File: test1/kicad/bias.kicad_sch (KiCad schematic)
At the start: 0 parts

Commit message: test1: fill in Power, Bias, Bobcat, Connectors, FMC sheets
Completes the test1 Bobcat carrier hierarchical schematic. All 7 sheets
(root + 6 children) parse cleanly with kicad-cli and render to SVG/PDF.

Contents per child:
  - power.kicad_sch       — TPS7A8401A LDO (3P3V → 0.8V via ANY-OUT
                            strap, OUT side fans to +VDDD/+VDDA1/+VDDA2
                            via 1×2 jumpers) + TPS22916 load switch
                            (VADJ → +VDDIO) with EN pulldowns + decoupling.
  - bobcat.kicad_sch      — Bobcat 40-QFN DUT with VDDD/VDDIO decoupling,
                            VDDA1/VDDA2 series 0Ω + decoupling, hier-label
                            exits on all four edges for SAMPLE_OUT*,
                            SPI, GPIO, CLK_OUT*, BIAS0/1, etc.
  - eeprom.kicad_sch      — 24AA08 I²C EEPROM (address 000, WP→GND,
                            0.1 µF decoupling, 2.2 kΩ I²C pull-ups).
  - bias.kicad_sch        — MCP4728 quad DAC + OPA2388 dual op-amp
                            (units 1 & 2) + PMZ1200UPEYL high-side PMOS
                            × 2 channels + 5.11 kΩ 0.1% sense resistors +
                            DNP 2N7002 isolation NMOS placeholders.
  - connectors.kicad_sch  — 4× SMA for CLK_OUT0–3, 3× SMA for
                            OSC_EN/WEIGHT_EN/SAMPLE_TRIG, 1×4 GPIO
                            header, 3× Keystone-5011 GND test clips.
  - fmc.kicad_sch         — VITA 57.1 LPC connector (4 units × 40 pins),
                            wired for 3P3V/VADJ/SCL/SDA/PRSNT/GA0/GA1/
                            PG_C2M/LDO_EN/LSW_EN; LA-bank pins NC'd for
                            later pinning; all other C/D/G/H pins to GND.

Generator improvements driven by this round:
  - Multi-unit symbol support (parse_pins now returns the per-pin unit
    number; place() takes a unit= parameter and emits matching (unit N)
    in the instance + path).
  - Escape backslash/quote in property values so refs/values with
    embedded " (e.g. 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
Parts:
- added C1, C3, C4: 0.1uF, Capacitor_SMD:C_0402_1005Metric, symbol Device:C
- added C2: 10nF, Capacitor_SMD:C_0402_1005Metric, symbol Device:C
- added Q1, Q2: PMZ1200UPEYL, Package_DFN_QFN:DFN-3-1EP_1.0x1.0mm_P0.65mm_EP0.5x0.5mm, symbol Lib:PMZ1200UPEYL
- added Q3, Q4: 2N7002 (DNP), Package_TO_SOT_SMD:SOT-23, symbol Lib:2N7002
- added R1, R2: 5.11k 0.1%, Resistor_SMD:R_0402_1005Metric, symbol Device:R
- added U1: MCP4728, Package_DFN_QFN:VQFN-10-1EP_3x3mm_P0.5mm_EP1.6x1.6mm, symbol Lib:MCP4728
- added U2: OPA2388, Package_SO:SOIC-8_3.9x4.9mm_P1.27mm, symbol Lib:OPA2388
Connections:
- new net: U1.7 (VOUTB), U2.5 (+IN_B)
- new net: Q2.1 (G), U2.7 (OUT_B)
- new net: Q1.1 (G), U2.1 (OUT_A)
- new net: U1.6 (VOUTA), U2.3 (+IN_A)
- new net +3V3: C1.1, C2.1, C3.1, C4.1, R1.1, R2.1, U1.1 (VDD), U2.8 (V+)
- new net BIAS0: Q1.2 (S), Q1.3 (D), R1.2, U2.2 (-IN_A)
- new net BIAS1: Q2.2 (S), Q2.3 (D), R2.2, U2.6 (-IN_B)
- new net GND: C1.2, C2.2, C3.2, C4.2, U1.10 (VSS), U1.4 (*LDAC), U2.4 (V-)
- new net SCL: U1.2 (SCL)
- new net SDA: U1.3 (SDA)
- no-connect marks 0 -> 9

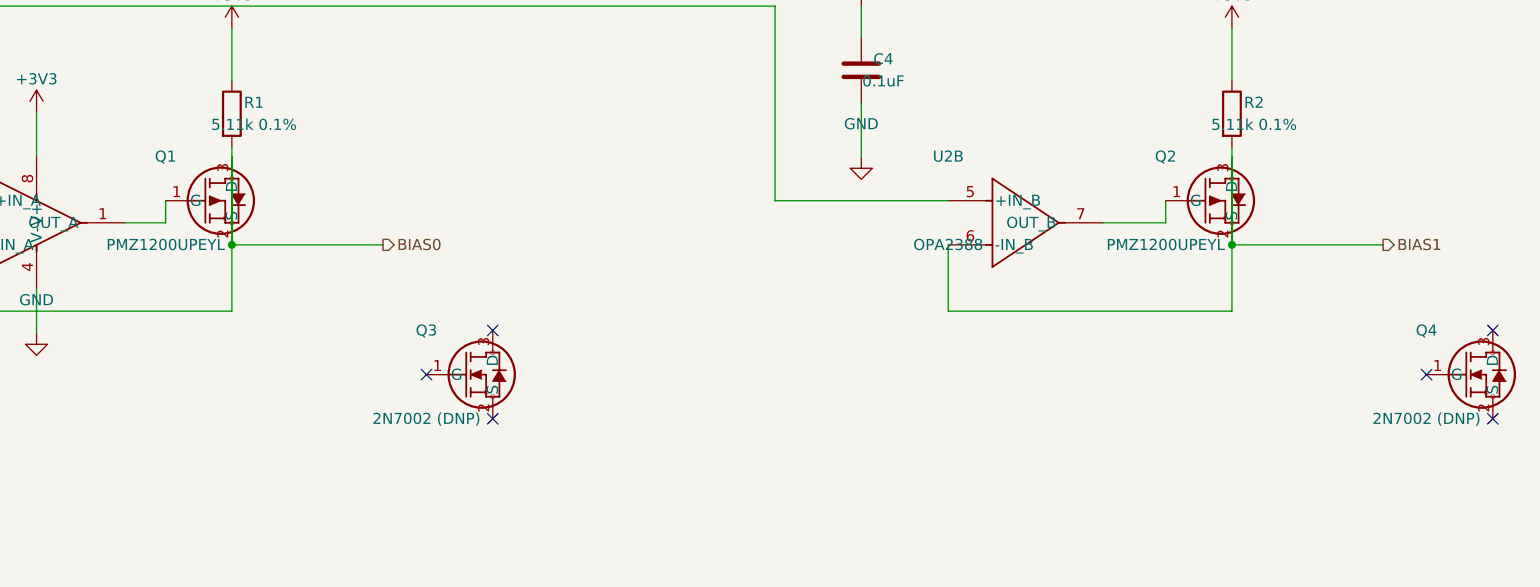
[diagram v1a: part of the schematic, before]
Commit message: Apply layout best-practices from reference schematic
Skill updates (from the LTC3114 reference sample):
  - New rule 5: no net passes through a component body (visual ambiguity).
  - New rule 6: every placed component is in-path or removed — DNP parts
    stay wired in series and just carry (dnp yes) + "DNP" value tag; never
    leave a part with no_connect on all its pins as a "for later"
    placeholder.
  - New rule 7: GND symbols cluster — one (power:GND) per local pin group,
    not one per pin. Connector banks bus their GNDs onto a single rail
    with one terminating triangle.
  - New rule 8: canonical decoupling-cap cluster (bulk+HF share one rail
    above and one GND below; stay off the path of unrelated nets).

test1 design fixes (each addresses a specific point raised on review):

  1. Bias: Q3, Q4 (2N7002 NMOS isolators) now wired in series between
     each PMOS drain and the BIASx output — gates exit as BIAS_ISO0 /
     BIAS_ISO1 hier labels for MCU control. Marked DNP via "2N7002 DNP"
     value. No more orphaned no_connects.

  2. Bobcat: VDDA2 decoupling cap C4 moved onto its own branch BELOW the
     R6 series-0Ω lane, off the pin-26/27 tie wire path.

  3. FMC: ~150 individual per-pin GND symbols collapsed into one
     consolidated GND rail per unit (J1/J2/J3/J4), each terminating in a
     single GND triangle at the rail's bottom.

  4. Power: TPS22916 (U2) decoupling caps C6 and C7 moved ALONGSIDE the
     chip body (left and right) at the same y as VIN/VOUT — wires no
     longer pass under the chip footprint. Cap pin 1 (top) → chip pin
     via horizontal stub; cap pin 2 (bot) → GND rail below.

Co-Authored-By: Claude Opus 4.7 (1M context) <noreply@anthropic.com>
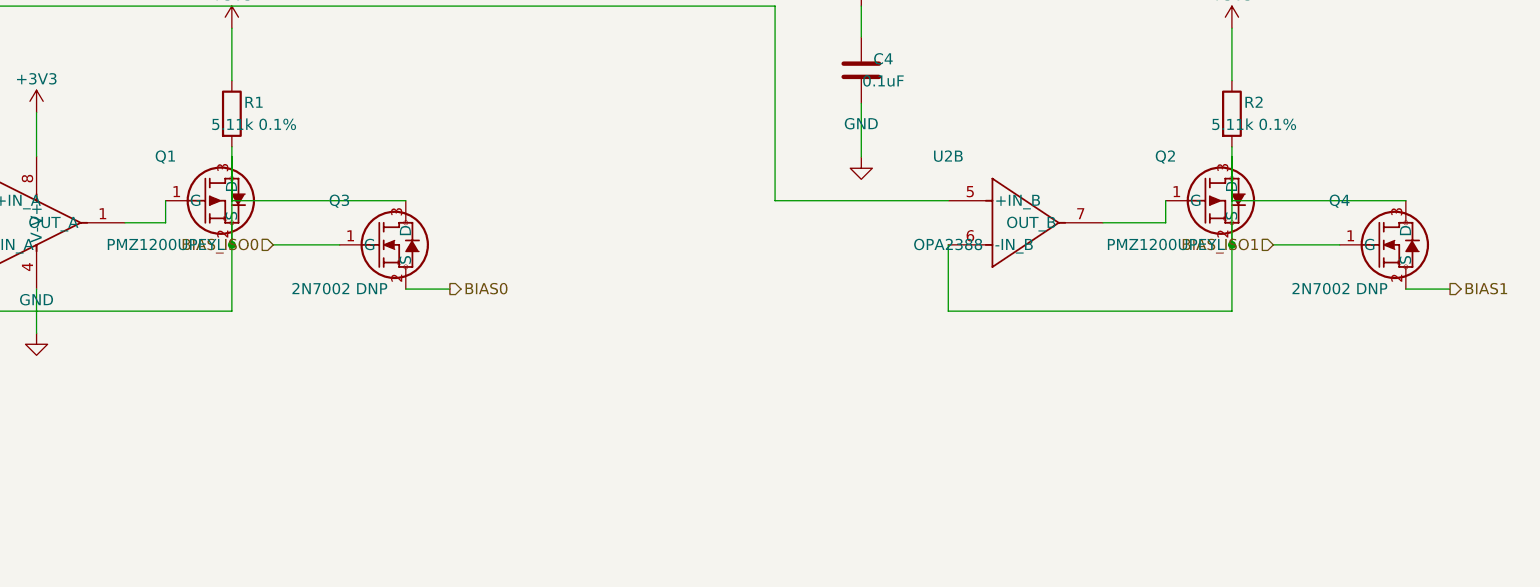
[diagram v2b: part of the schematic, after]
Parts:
- Q3, Q4: value 2N7002 (DNP) -> 2N7002 DNP
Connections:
- net BIAS0: now also Q3.2 (S); no longer Q1.2 (S), Q1.3 (D), R1.2, U2.2 (-IN_A)
- net BIAS1: now also Q4.2 (S); no longer Q2.2 (S), Q2.3 (D), R2.2, U2.6 (-IN_B)
- net BIAS_ISO0: now reaches Q3.1 (G)
- net at Q3.3 (D): now also Q1.2 (S), Q1.3 (D), R1.2, U2.2 (-IN_A)
- net BIAS_ISO1: now reaches Q4.1 (G)
- net at Q4.3 (D): now also Q2.2 (S), Q2.3 (D), R2.2, U2.6 (-IN_B)
- no-connect marks 9 -> 3
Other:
- moved on the sheet: Q3, Q4
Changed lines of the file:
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@@
   (wire (pts (xy 237.62 122.7) (xy 237.62 115.08)) (stroke (width 0) (type default)))
   (junction (at 237.62 115.08) (diameter 0) (color 0 0 0 0))
-  (wire (pts (xy 237.62 104.92) (xy 237.62 115.08)) (stroke (width 0) (type default)))
-  (wire (pts (xy 237.62 115.08) (xy 255 115.08)) (stroke (width 0) (type default)))
-  (hierarchical_label "BIAS0" (shape output) (at 255 115.08 0) (effects (font (size 1.27 1.27)) (justify left)))
   (symbol
     (lib_id "Lib:2N7002")
-    (at 260 130 0)
+    (at 250 115.08 0)
     (unit 1) (in_bom yes) (on_board yes) (dnp no)
-    (property "Reference" "Q3" (at 260 124.92 0) (effects (font (size 1.27 1.27))))
-    (property "Value" "2N7002 (DNP)" (at 260 135.08 0) (effects (font (size 1.27 1.27))))
+    (property "Reference" "Q3" (at 250 110.0 0) (effects (font (size 1.27 1.27))))
+    (property "Value" "2N7002 DNP" (at 250 120.16 0) (effects (font (size 1.27 1.27))))
     (property "Footprint" "Package_TO_SOT_SMD:SOT-23" (at 0 0 0) (effects (font (size 1.27 1.27)) (hide yes)))
     (property "Datasheet" "" (at 0 0 0) (effects (font (size 1.27 1.27)) (hide yes)))
@@
       (project "test1"
         (path "/4ed7a046-ef33-57d9-8730-321c05965af3/ddf1c49f-55ac-530a-9ee4-38ad9d14caf8" (reference "Q3") (unit 1)))))
-  (no_connect (at 260.0 130.0))
-  (no_connect (at 267.62 135.08))
-  (no_connect (at 267.62 124.92))
+  (wire (pts (xy 237.62 104.92) (xy 237.62 110.0)) (stroke (width 0) (type default)))
+  (wire (pts (xy 237.62 110.0) (xy 257.62 110.0)) (stroke (width 0) (type default)))
+  (wire (pts (xy 257.62 120.16) (xy 262.7 120.16)) (stroke (width 0) (type default)))
+  (hierarchical_label "BIAS0" (shape output) (at 262.7 120.16 0) (effects (font (size 1.27 1.27)) (justify left)))
+  (wire (pts (xy 250.0 115.08) (xy 242.38 115.08)) (stroke (width 0) (type default)))
+  (hierarchical_label "BIAS_ISO0" (shape input) (at 242.38 115.08 180) (effects (font (size 1.27 1.27)) (justify right)))
   (wire (pts (xy 215.16 104.92) (xy 215.16 99.84)) (stroke (width 0) (type default)))
   (symbol
@@
   (wire (pts (xy 352.62 122.7) (xy 352.62 115.08)) (stroke (width 0) (type default)))
   (junction (at 352.62 115.08) (diameter 0) (color 0 0 0 0))
-  (wire (pts (xy 352.62 104.92) (xy 352.62 115.08)) (stroke (width 0) (type default)))
-  (wire (pts (xy 352.62 115.08) (xy 370 115.08)) (stroke (width 0) (type default)))
-  (hierarchical_label "BIAS1" (shape output) (at 370 115.08 0) (effects (font (size 1.27 1.27)) (justify left)))
   (symbol
     (lib_id "Lib:2N7002")
-    (at 375 130 0)
+    (at 365 115.08 0)
     (unit 1) (in_bom yes) (on_board yes) (dnp no)
-    (property "Reference" "Q4" (at 375 124.92 0) (effects (font (size 1.27 1.27))))
-    (property "Value" "2N7002 (DNP)" (at 375 135.08 0) (effects (font (size 1.27 1.27))))
+    (property "Reference" "Q4" (at 365 110.0 0) (effects (font (size 1.27 1.27))))
+    (property "Value" "2N7002 DNP" (at 365 120.16 0) (effects (font (size 1.27 1.27))))
     (property "Footprint" "Package_TO_SOT_SMD:SOT-23" (at 0 0 0) (effects (font (size 1.27 1.27)) (hide yes)))
     (property "Datasheet" "" (at 0 0 0) (effects (font (size 1.27 1.27)) (hide yes)))
@@
       (project "test1"
         (path "/4ed7a046-ef33-57d9-8730-321c05965af3/ddf1c49f-55ac-530a-9ee4-38ad9d14caf8" (reference "Q4") (unit 1)))))
-  (no_connect (at 375.0 130.0))
-  (no_connect (at 382.62 135.08))
-  (no_connect (at 382.62 124.92))
+  (wire (pts (xy 352.62 104.92) (xy 352.62 110.0)) (stroke (width 0) (type default)))
+  (wire (pts (xy 352.62 110.0) (xy 372.62 110.0)) (stroke (width 0) (type default)))
+  (wire (pts (xy 372.62 120.16) (xy 377.7 120.16)) (stroke (width 0) (type default)))
+  (hierarchical_label "BIAS1" (shape output) (at 377.7 120.16 0) (effects (font (size 1.27 1.27)) (justify left)))
+  (wire (pts (xy 365.0 115.08) (xy 357.38 115.08)) (stroke (width 0) (type default)))
+  (hierarchical_label "BIAS_ISO1" (shape input) (at 357.38 115.08 180) (effects (font (size 1.27 1.27)) (justify right)))
   (symbol
     (lib_id "Device:C")

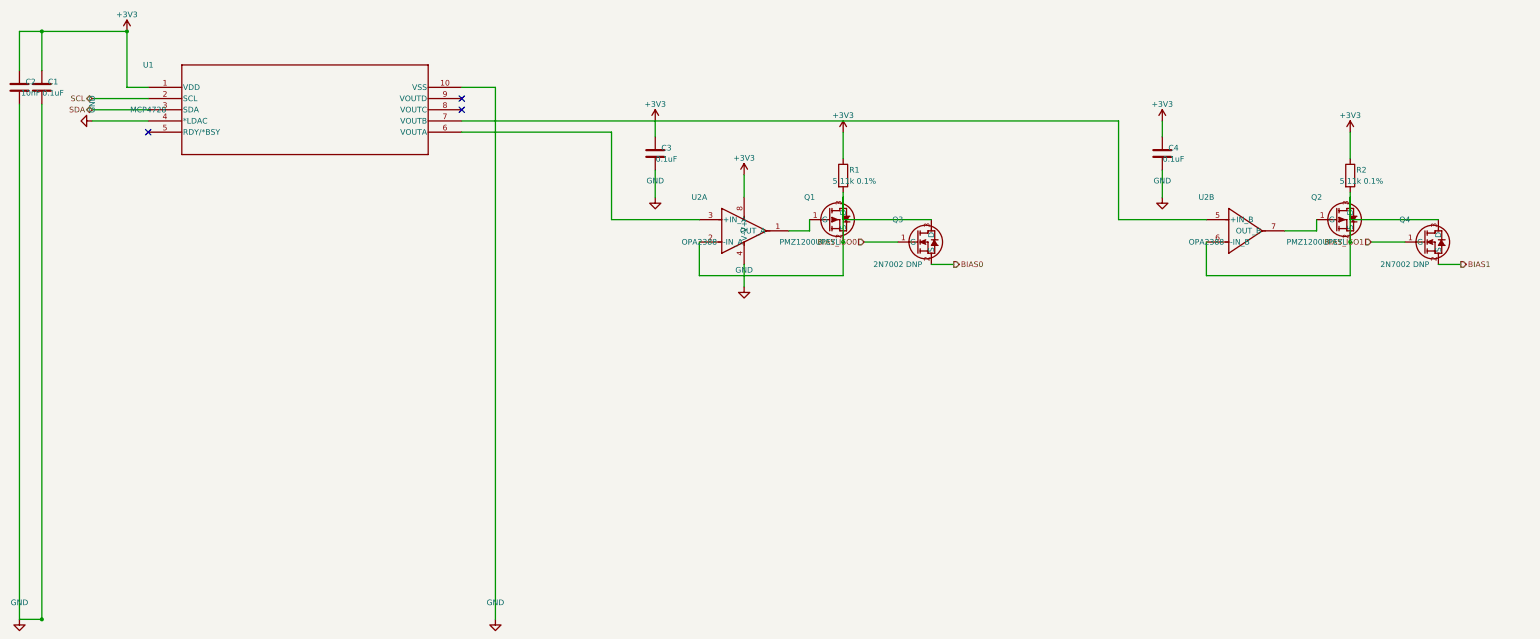
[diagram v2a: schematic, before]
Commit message: Project-wide connectivity audit: refdes uniqueness + hier-label correctness
Added test1/verify_project.py as a kicad-cli-erc substitute (the dev
build doesn't ship _cvpcb.kiface, so sch erc is broken). The verifier
parses all .kicad_sch files and checks:
  1. Duplicate refdes (KiCad's refdes namespace is project-wide).
  2. Parent sheet-pin name + direction matches child hierarchical_label.
  3. Orphan child hierarchical_labels (no matching parent pin).

First run flagged 48 issues. Now reports 0.

Refdes scheme — per-sheet decade ranges so global namespace stays unique:
  FMC 1-9 (J1-J4)
  Power 10-19 (U10/U11, R10/R11, C10-C16, J10-J12)
  Bobcat 20-29 (U20, R20/R21, C20-C25)
  EEPROM 30-39 (U30, R30/R31, C30)
  Bias 40-49 (U40/U41 [U41 dual-unit OPA], Q40-Q43, R40/R41, C40-C43)
  Connectors 50-59 (J50-J57, TP50-TP52)

Hierarchical / global label rework:
  - Parent sheet-pin directions corrected to match child labels (was
    flipped on every Bobcat SPI pin and on FMC's LDO_EN/LSW_EN/LDO_PG).
  - Bobcat SPI labels: passive → input/output as appropriate.
  - Project-wide nets converted to global_label (auto-tie by name, no
    parent pins): SCL, SDA, SAMPLE_OUT*, OSC_EN, WEIGHT_EN, SAMPLE_TRIG,
    BIAS_ISO0/1, CS_L, SCLK, MOSI, MISO, SPI_DMODE, RESET_N.
  - hier_label retained for clean 2-sheet pairs: VADJ, LDO_EN, LDO_PG,
    LSW_EN (FMC ↔ Power); BIAS0/1 (Bias ↔ Bobcat); CLK_OUT0-3, GPIO0-3
    (Bobcat ↔ Connectors).
  - Visual cue in renders: globals render as boxed rectangles; hierarchical
    labels render as arrows — handy when scanning a sheet.

Memory: appended five connectivity-correctness lessons to
feedback_kicad_generator_lessons.md (refdes namespace, parent/child
direction parity, no-passive-for-real-signals, global vs hier decision
table, verify-after-every-change).

Co-Authored-By: Claude Opus 4.7 (1M context) <noreply@anthropic.com>
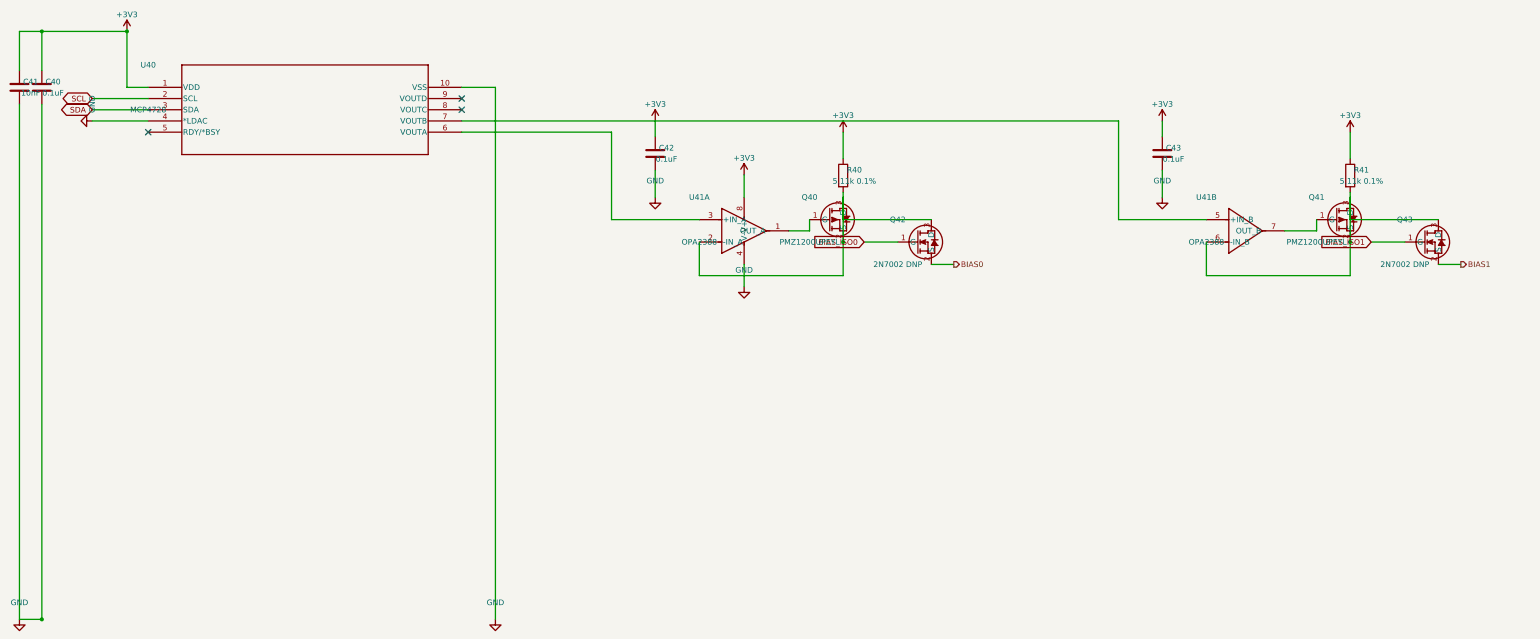
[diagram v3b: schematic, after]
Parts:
- removed C1, C3, C4: 0.1uF, Capacitor_SMD:C_0402_1005Metric, symbol Device:C
- removed C2: 10nF, Capacitor_SMD:C_0402_1005Metric, symbol Device:C
- removed Q1, Q2: PMZ1200UPEYL, Package_DFN_QFN:DFN-3-1EP_1.0x1.0mm_P0.65mm_EP0.5x0.5mm, symbol Lib:PMZ1200UPEYL
- removed Q3, Q4: 2N7002 DNP, Package_TO_SOT_SMD:SOT-23, symbol Lib:2N7002
- removed R1, R2: 5.11k 0.1%, Resistor_SMD:R_0402_1005Metric, symbol Device:R
- removed U1: MCP4728, Package_DFN_QFN:VQFN-10-1EP_3x3mm_P0.5mm_EP1.6x1.6mm, symbol Lib:MCP4728
- removed U2: OPA2388, Package_SO:SOIC-8_3.9x4.9mm_P1.27mm, symbol Lib:OPA2388
- added C40, C42, C43: 0.1uF, Capacitor_SMD:C_0402_1005Metric, symbol Device:C
- added C41: 10nF, Capacitor_SMD:C_0402_1005Metric, symbol Device:C
- added Q40, Q41: PMZ1200UPEYL, Package_DFN_QFN:DFN-3-1EP_1.0x1.0mm_P0.65mm_EP0.5x0.5mm, symbol Lib:PMZ1200UPEYL
- added Q42, Q43: 2N7002 DNP, Package_TO_SOT_SMD:SOT-23, symbol Lib:2N7002
- added R40, R41: 5.11k 0.1%, Resistor_SMD:R_0402_1005Metric, symbol Device:R
- added U40: MCP4728, Package_DFN_QFN:VQFN-10-1EP_3x3mm_P0.5mm_EP1.6x1.6mm, symbol Lib:MCP4728
- added U41: OPA2388, Package_SO:SOIC-8_3.9x4.9mm_P1.27mm, symbol Lib:OPA2388
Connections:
- net +3V3: now also C40.1, C41.1, C42.1, C43.1, R40.1, R41.1, U40.1 (VDD), U41.8 (V+)
- net BIAS0: now also Q42.2 (S)
- net BIAS1: now also Q43.2 (S)
- net BIAS_ISO0: now also Q42.1 (G)
- net BIAS_ISO1: now also Q43.1 (G)
- net GND: now also C40.2, C41.2, C42.2, C43.2, U40.10 (VSS), U40.4 (*LDAC), U41.4 (V-)
- net SCL: now also U40.2 (SCL)
- net SDA: now also U40.3 (SDA)
- new net: Q41.1 (G), U41.7 (OUT_B)
- new net: Q41.2 (S), Q41.3 (D), Q43.3 (D), R41.2, U41.6 (-IN_B)
- new net: Q40.1 (G), U41.1 (OUT_A)
- new net: Q40.2 (S), Q40.3 (D), Q42.3 (D), R40.2, U41.2 (-IN_A)
- new net: U40.6 (VOUTA), U41.3 (+IN_A)
- new net: U40.7 (VOUTB), U41.5 (+IN_B)
